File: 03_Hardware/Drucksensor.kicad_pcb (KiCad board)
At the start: 2 copper layers, 160 x 100 mm, 192 parts, among them J101 24V in, J103 RS485-mini-1, J104 RJ45, J108 RJ45, J109 RJ45, J110 DS18B20, J111 BMP280, J112 RJ45, J113 RS485-mini-1, J114 AVR-ISP-6, J401 Conn_01x03, J402 Conn_01x03, J403 Conn_01x02, J404 Conn_01x02, K401 V23040, K402 V23040, Q1 BC817, Q2 BC817, Q201 BC807, Q401 BC817, Q402 BC817, SW101 SW_Omron_B3FS, SW102 SW_Omron_B3FS, SW103 SW_DIP_x08, SW104 SW_Omron_B3FS, U103 ATmega8A-A, U104 REF3040, U105 74HC165, U106 74HC595, U107 SN75176AD, U108 CAT24M01W, U201 8106BS, U202 74HC595, U203 8106BS, U204 74HC595, U205 8106BS, U206 74HC595, U207 5161BK, U208 74HC595, U209 74HC595, U210 5161BK, U211 74HC595, U301 TPS54202DDC, U302 AP1117-33, U401 CPC1002N, U402 CPC1002N, Y101 16MHz

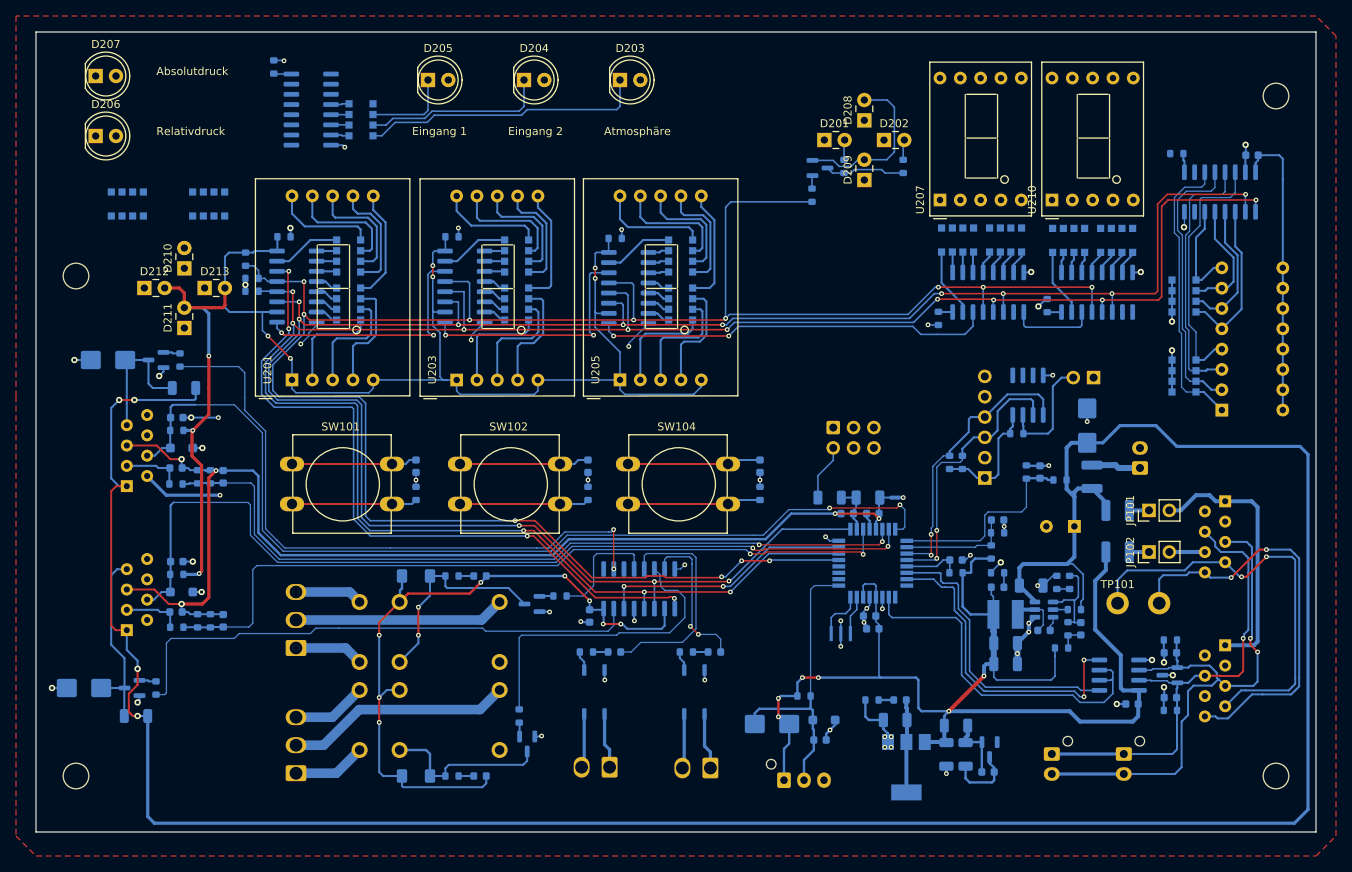
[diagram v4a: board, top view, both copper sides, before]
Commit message: Layout aktuell fast DRC-Fehlerfrei, Überlappungen von Plus-Zeichen sind in Ordnung. Texte müssen noch ausgerichtet werden!
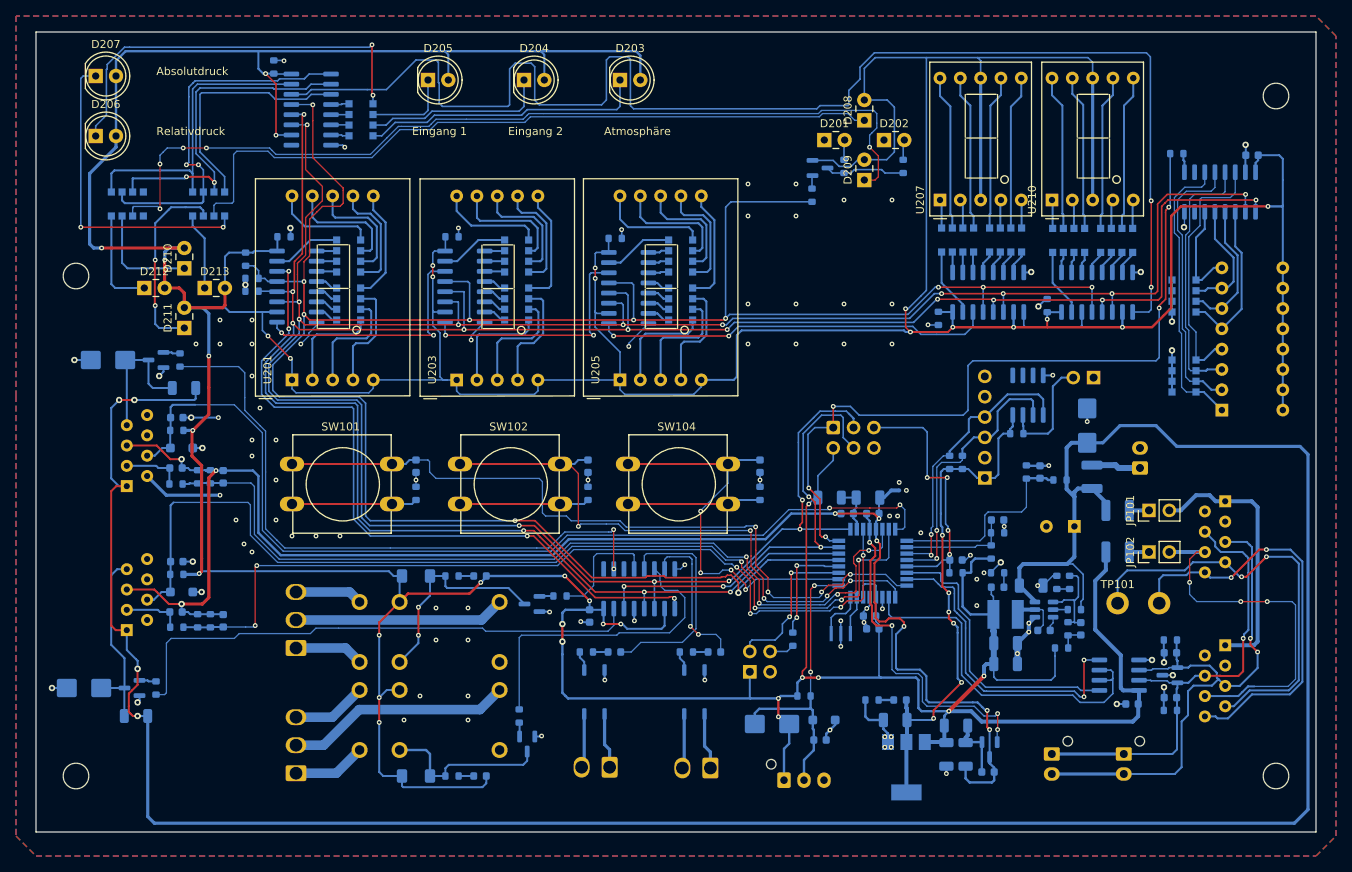
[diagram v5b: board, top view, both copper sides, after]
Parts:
- added J102: Conn_01x04, Connector_PinHeader_2.54mm:PinHeader_2x02_P2.54mm_Vertical, B.Cu at (129.2, 132.0)
- added R108: 1k, Resistor_SMD:R_0603_1608Metric, B.Cu at (134.6, 127.9)
- moved NT101 0.90 mm to (147.4, 109.3)
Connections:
- U207 pad 1: Net-(RN208-R4.2) -> Net-(RN207-R4.2)
- U207 pad 10: Net-(RN208-R2.2) -> Net-(RN207-R3.2)
- U207 pad 2: Net-(RN207-R1.2) -> Net-(RN207-R2.2)
- U207 pad 4: Net-(RN207-R2.2) -> Net-(RN208-R3.2)
- U207 pad 6: Net-(RN207-R3.2) -> Net-(RN208-R2.2)
- U207 pad 7: Net-(RN207-R4.2) -> Net-(RN208-R4.2)
- U207 pad 9: Net-(RN208-R3.2) -> Net-(RN207-R1.2)
- U210 pad 1: Net-(RN210-R4.2) -> Net-(RN209-R4.2)
- U210 pad 10: Net-(RN210-R2.2) -> Net-(RN209-R3.2)
- U210 pad 2: Net-(RN209-R1.2) -> Net-(RN209-R2.2)
- U210 pad 4: Net-(RN209-R2.2) -> Net-(RN210-R3.2)
- U210 pad 6: Net-(RN209-R3.2) -> Net-(RN210-R2.2)
- U210 pad 7: Net-(RN209-R4.2) -> Net-(RN210-R4.2)
- U210 pad 9: Net-(RN210-R3.2) -> Net-(RN209-R1.2)
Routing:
- net +5V: track 500.1 -> 931.8 mm, vias 23 -> 37
- net Net-(U209-QH'): track 0.00 -> 174.6 mm, vias 0 -> 2
- net /7-Segment/ExponentVorzeichenVert1: track 0.00 -> 114.8 mm, vias 0 -> 5
- net /MISO_Schieber_Daten_In: track 1.86 -> 95.5 mm, vias 1 -> 5
- net /7-Segment/ExponentVorzeichenVert2: track 0.00 -> 91.9 mm
- net /Ext_INT0_Taster_1: track 15.7 -> 93.6 mm, vias 0 -> 4
- net /Ext_INT1_Taster_2: track 16.2 -> 76.0 mm, vias 0 -> 5
- net /7-Segment/AnzeigeRelativdruck: track 0.00 -> 51.1 mm, vias 0 -> 2
- net /SCK_Schieber_Takt: track 259.8 -> 308.2 mm, vias 12 -> 15
- net Net-(RN211-R2.1): track 0.00 -> 46.1 mm, vias 0 -> 2
- net GNDA: track 156.2 -> 199.8 mm, vias 5 -> 9
- net Net-(RN211-R3.1): track 0.00 -> 43.1 mm, vias 0 -> 2
- net Net-(JP102-B): track 4.45 -> 46.4 mm, vias 0 -> 3
- net Net-(U103-AREF): track 2.11 -> 43.5 mm, vias 0 -> 4
- net /7-Segment/AnzeigeAbsolutdruck: track 0.00 -> 39.9 mm, vias 0 -> 2
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- added copper zone on B.Cu, net GND

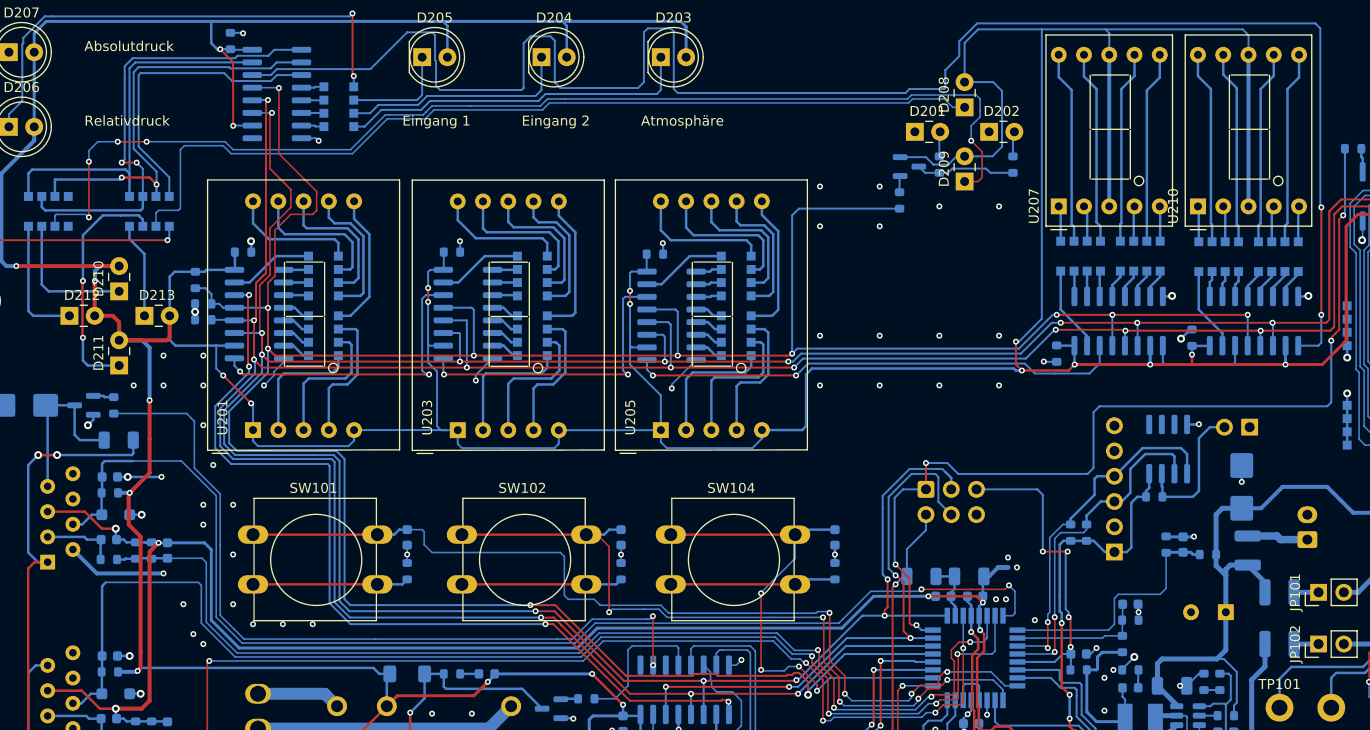
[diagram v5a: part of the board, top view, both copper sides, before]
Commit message: Texte ausgerichtet.
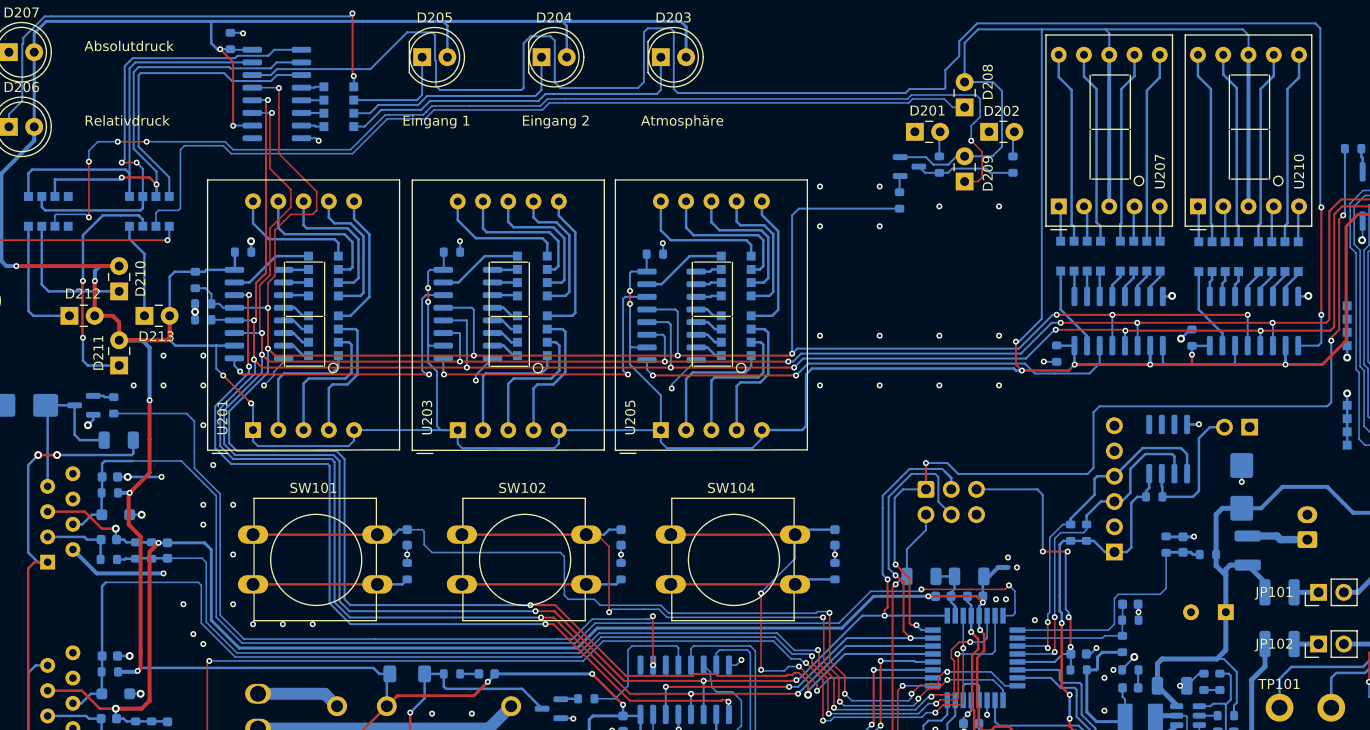
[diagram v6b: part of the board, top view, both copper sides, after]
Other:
- board text added: "Vakuumanzeige v02 - PhilippH - 11/2023 Nach einer Idee von: David und Sven"

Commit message: Software weitergemacht
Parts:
- C201, C202, C203, C204, C205, C206: footprint Resistor_SMD:R_0603_1608Metric -> Capacitor_SMD:C_0603_1608Metric
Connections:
- U108 pad 2: unconnected-(U108-A1-Pad2) -> GND
- U108 pad 3: unconnected-(U108-A2-Pad3) -> GND
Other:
- board text added: "Addr. LSB"
